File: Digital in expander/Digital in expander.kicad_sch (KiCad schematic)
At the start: 60 parts, among them J1 Screw_Terminal_01x02, J10 Screw_Terminal_01x02, J11 Screw_Terminal_01x02, J12 Screw_Terminal_01x02, J13 Screw_Terminal_01x02, J14 Screw_Terminal_01x02, J15 Screw_Terminal_01x02, J16 Screw_Terminal_01x02, J17 Conn_01x04_Pin, J18 Conn_01x04_Pin, J19 Conn_01x04_Pin, J2 Screw_Terminal_01x02, J20 Conn_01x04_Pin, J21 Conn_01x04_Pin, J22 Conn_01x03_Pin, J3 Screw_Terminal_01x02, J4 Screw_Terminal_01x02, J5 Screw_Terminal_01x02, J6 Screw_Terminal_01x02, J7 Screw_Terminal_01x02, J8 Screw_Terminal_01x02, J9 Screw_Terminal_01x02, U1 PC847, U2 PC847, U3 PC847, U4 PC847, U5 MCP23017_SO

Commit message: Nu borde det fungera bättre
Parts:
- removed J1, J10, J11, J12, J13, J14, J15, J16, J2, J3, J4, J5, J6, J7, J8, J9: Screw_Terminal_01x02, symbol Connector:Screw_Terminal_01x02
- removed R18, R21, R24, R25, R26, R27, R28, R29, R30, R31, R32: 4,7k, symbol Device:R
- added J1, J2: Screw_Terminal_01x16, symbol Connector:Screw_Terminal_01x16
- added J3, J4: Conn_01x15_Pin, symbol Connector:Conn_01x15_Pin
- added R1, R10, R11, R13, R14, R16, R2, R4, R5, R7, R8: 4,7k, symbol Device:R
- renumbered J19 to J10, J20 to J5, J21 to J6, J22 to J7, J17 to J8, J18 to J9, R4 to R12, R5 to R15, R6 to R18, R7 to R21, R8 to R24, R9 to R25, R10 to R26, R11 to R27, R12 to R28, R13 to R29, R1 to R3, R14 to R30, R15 to R31, R16 to R32, R2 to R6, R3 to R9
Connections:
- net at U1.15, U5.1 (GPB0): now also R1.1; no longer R17.1
- net at C1.2, J10.1 (Pin_1), J10.2 (Pin_2)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: now also R1.2, R10.2, R11.2, R13.2, R14.2, R16.2, R2.2, R4.2, R5.2, R7.2, R8.2
- net at U2.15, U5.5 (GPB4): now also R7.1
- net at R15.1: now also J1.5 (Pin_5)
- net at U1.10, U1.12, U1.14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: no longer C1.1, J5.1 (Pin_1), J6.1 (Pin_1), J8.1 (Pin_1), J8.2 (Pin_2), J8.3 (Pin_3), J8.4 (Pin_4), U5.9 (VDD)
- net at R26.1: now also J1.10 (Pin_10)
- net at U4.15, U5.25 (GPA4): now also R19.1
- net at U4.2: now also J2.13 (Pin_13), J3.12 (Pin_12)
- net at R32.1: now also J1.16 (Pin_16)
- net at U4.8: now also J2.16 (Pin_16), J3.15 (Pin_15)
- net at U4.9, U5.28 (GPA7): now also R23.1
- net at R30.1: now also J1.14 (Pin_14)
- net at U4.4: now also J2.14 (Pin_14), J3.13 (Pin_13)
- net at U5.15 (A0): now also J9.2 (Pin_2); no longer J9.1 (Pin_1)
- net at U5.16 (A1): now also J9.3 (Pin_3); no longer J9.2 (Pin_2)
- net at U5.17 (A2): now also J9.4 (Pin_4); no longer J9.3 (Pin_3)
- net at J7.3 (Pin_3), U5.18 (~{RESET}): now also J9.1 (Pin_1); no longer J9.4 (Pin_4)
- net at U1.13, U5.2 (GPB1): now also R2.1
- net at U3.15, U5.21 (GPA0): now also R13.1
- net at U3.13, U5.22 (GPA1): now also R14.1
- net at U3.11, U5.23 (GPA2): now also R16.1
- net at U3.9, U5.24 (GPA3): now also R17.1
- net at U4.13, U5.26 (GPA5): now also R20.1
- net at U4.11, U5.27 (GPA6): now also R22.1
- net at U1.11, U5.3 (GPB2): now also R4.1; no longer R19.1
- net at U1.9, U5.4 (GPB3): now also R5.1; no longer R20.1
- net at U2.13, U5.6 (GPB5): now also R8.1; no longer R22.1
- net at U2.11, U5.7 (GPB6): now also R10.1; no longer R23.1
- net at U2.9, U5.8 (GPB7): now also R11.1
- net at R3.1: now also J1.1 (Pin_1)
- net at R25.1: now also J1.9 (Pin_9)
- net at R28.1: now also J1.12 (Pin_12)
- net at R27.1: now also J1.11 (Pin_11)
- net at U3.6: now also J2.11 (Pin_11), J3.10 (Pin_10)
- net at R24.1: now also J1.8 (Pin_8)
- net at R9.1: now also J1.3 (Pin_3)
- net at U1.6: now also J2.3 (Pin_3), J3.2 (Pin_2)
- net at U3.4: now also J2.10 (Pin_10), J3.9 (Pin_9)
- net at U2.8: now also J2.8 (Pin_8), J3.7 (Pin_7)
- net at U2.2: now also J2.5 (Pin_5), J3.4 (Pin_4)
- net at R29.1: now also J1.13 (Pin_13)
- net at U1.2: now also U1.4, J2.2 (Pin_2), J3.1 (Pin_1)
- net at R21.1: now also J1.7 (Pin_7)
- net at U2.6: now also J2.7 (Pin_7), J3.6 (Pin_6)
- net at R6.1: now also J1.2 (Pin_2)
- net at R12.1: now also J1.4 (Pin_4)
- net at U1.8: now also J2.4 (Pin_4), J3.3 (Pin_3)
- net at U2.4: now also J2.6 (Pin_6), J3.5 (Pin_5)
- net at U4.6: now also J2.15 (Pin_15), J3.14 (Pin_14)
- net at U3.8: now also J2.12 (Pin_12), J3.11 (Pin_11)
- net at U3.2: now also J2.9 (Pin_9), J3.8 (Pin_8)
- net at R18.1: now also J1.6 (Pin_6)
- net at R31.1: now also J1.15 (Pin_15)
- new net: J2.1 (Pin_1), J4.1 (Pin_1), J4.10 (Pin_10), J4.11 (Pin_11), J4.12 (Pin_12), J4.13 (Pin_13), J4.14 (Pin_14), J4.15 (Pin_15), J4.2 (Pin_2), J4.3 (Pin_3), J4.4 (Pin_4), J4.5 (Pin_5), J4.6 (Pin_6), J4.7 (Pin_7), J4.8 (Pin_8), J4.9 (Pin_9)
- new net: C1.1, J5.1 (Pin_1), J6.1 (Pin_1), J8.1 (Pin_1), J8.2 (Pin_2), J8.3 (Pin_3), J8.4 (Pin_4), U5.9 (VDD)
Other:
- note added: "GND 1 (C)"
- note added: "GND 10"
- note added: "GND 11"
- note added: "GND 12"
- note added: "GND 13"
- note added: "GND 14"
- note added: "GND 15"
- note added: "GND 16"
- note added: "GND 2"
- note added: "GND 3"
- note added: "GND 4"
- note added: "GND 5"
- note added: "GND 6"
- note added: "GND 7"
- note added: "GND 8"
- note added: "GND 9"
- moved on the sheet: C1, J10, J5, J6, J7, J8, J9, R12, R15, R18, R21, R24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

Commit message: Förbättrad läsbarhet
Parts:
- R1, R10, R11, R13, R14, R16, R2, R4, R5, R7, R8: value 4,7k -> 1k
- R18, R21, R24, R25, R26, R27, R28, R29, R30, R31, R32: value 1k -> 4,7k
- renumbered J7 to J10, J8 to J5, J9 to J6, J10 to J7, J5 to J8, J6 to J9
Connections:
- net at J4.1 (Pin_1), J4.10 (Pin_10), J4.11 (Pin_11)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: now also J1.1 (Pin_1), U1.2; no longer J2.1 (Pin_1)
- net at J3.9 (Pin_9), U3.4: now also J1.10 (Pin_10); no longer J2.10 (Pin_10)
- net at J3.10 (Pin_10), U3.6: now also J1.11 (Pin_11); no longer J2.11 (Pin_11)
- net at J3.11 (Pin_11), U3.8: now also J1.12 (Pin_12); no longer J2.12 (Pin_12)
- net at J3.12 (Pin_12), U4.2: now also J1.13 (Pin_13); no longer J2.13 (Pin_13)
- net at J3.13 (Pin_13), U4.4: now also J1.14 (Pin_14); no longer J2.14 (Pin_14)
- net at J3.14 (Pin_14), U4.6: now also J1.15 (Pin_15); no longer J2.15 (Pin_15)
- net at J3.15 (Pin_15), U4.8: now also J1.16 (Pin_16); no longer J2.16 (Pin_16)
- net at J3.1 (Pin_1), U1.4: now also J1.2 (Pin_2); no longer J2.2 (Pin_2), U1.2
- net at J3.2 (Pin_2), U1.6: now also J1.3 (Pin_3); no longer J2.3 (Pin_3)
- net at J3.3 (Pin_3), U1.8: now also J1.4 (Pin_4); no longer J2.4 (Pin_4)
- net at J3.4 (Pin_4), U2.2: now also J1.5 (Pin_5); no longer J2.5 (Pin_5)
- net at J3.5 (Pin_5), U2.4: now also J1.6 (Pin_6); no longer J2.6 (Pin_6)
- net at J3.6 (Pin_6), U2.6: now also J1.7 (Pin_7); no longer J2.7 (Pin_7)
- net at J3.7 (Pin_7), U2.8: now also J1.8 (Pin_8); no longer J2.8 (Pin_8)
- net at J3.8 (Pin_8), U3.2: now also J1.9 (Pin_9); no longer J2.9 (Pin_9)
- net at R15.1: now also J2.15 (Pin_15); no longer J1.5 (Pin_5)
- net at R15.2: now also U4.5; no longer U2.1
- net at C1.1, J5.1 (Pin_1), J5.2 (Pin_2)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: now also U1.10, U1.12, U1.14, U1.16, U2.10, U2.12, U2.14, U2.16, U3.10, U3.12, U3.14, U3.16, U4.10, U4.12, U4.14, U4.16
- net at C1.2, J7.1 (Pin_1), J7.2 (Pin_2)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: now also R18.2, R21.2, R24.2, R25.2, R26.2, R27.2, R28.2, R29.2, R30.2, R31.2, R32.2; no longer R1.2, R10.2, R11.2, R13.2, R14.2, R16.2, R2.2, R4.2, R5.2, R7.2, R8.2
- net at R26.1: now also U3.13, U5.22 (GPA1); no longer J1.10 (Pin_10)
- net at U3.3: now also R10.2; no longer R26.2
- net at U3.15, U5.21 (GPA0): now also R25.1; no longer R13.1
- net at U4.1: now also R13.2; no longer R29.2
- net at U4.15, U5.25 (GPA4): now also R29.1; no longer R19.1
- net at U2.11, U5.7 (GPB6): now also R23.1; no longer R10.1
- net at U1.15, U5.1 (GPB0): now also R17.1; no longer R1.1
- net at U5.15 (A0): now also J6.1 (Pin_1); no longer J6.2 (Pin_2)
- net at U5.16 (A1): now also J6.2 (Pin_2); no longer J6.3 (Pin_3)
- net at U5.17 (A2): now also J6.3 (Pin_3); no longer J6.4 (Pin_4)
- net at J10.3 (Pin_3), U5.18 (~{RESET}): now also J6.4 (Pin_4); no longer J6.1 (Pin_1)
- net at U1.13, U5.2 (GPB1): now also R18.1; no longer R2.1
- net at U3.11, U5.23 (GPA2): now also R27.1; no longer R16.1
- net at U3.9, U5.24 (GPA3): now also R28.1; no longer R17.1
- net at U4.13, U5.26 (GPA5): now also R30.1; no longer R20.1
- net at U4.11, U5.27 (GPA6): now also R31.1; no longer R22.1
- net at U4.9, U5.28 (GPA7): no longer R23.1
- net at U1.11, U5.3 (GPB2): now also R19.1; no longer R4.1
- net at U1.9, U5.4 (GPB3): now also R20.1; no longer R5.1
- net at U2.15, U5.5 (GPB4): now also R21.1; no longer R7.1
- net at U2.13, U5.6 (GPB5): now also R22.1; no longer R8.1
- net at U2.9, U5.8 (GPB7): now also R24.1; no longer R11.1
- net at R3.1: now also J2.3 (Pin_3); no longer J1.1 (Pin_1)
- net at U1.1: now also R1.2; no longer R3.2
- net at U3.1: now also R9.2; no longer R25.2
- net at U3.7: now also R12.2; no longer R28.2
- net at U2.7: now also R8.2; no longer R24.2
- net at R6.1: now also J2.6 (Pin_6); no longer J1.2 (Pin_2)
- net at R6.2: now also U2.3; no longer U1.3
- net at R32.1: no longer J1.16 (Pin_16)
- net at R9.1: now also J2.9 (Pin_9); no longer J1.3 (Pin_3)
- net at R12.1: now also J2.12 (Pin_12); no longer J1.4 (Pin_4)
- net at U4.3: now also R14.2; no longer R30.2
- net at U4.7: now also R16.2; no longer R32.2
- net at U2.5: now also R7.2; no longer R21.2
- net at U3.5: now also R11.2; no longer R27.2
- net at U1.7: now also R4.2; no longer R12.2
- net at U1.5: now also R3.2; no longer R9.2
- new net: J2.10 (Pin_10), R10.1
- new net: J2.5 (Pin_5), R5.1
- new net: R5.2, U2.1
- new net: R2.2, U1.3
- new net: J2.8 (Pin_8), R8.1
- new net: J2.1 (Pin_1), R1.1
- new net: J2.13 (Pin_13), R13.1
- new net: J2.16 (Pin_16), R16.1
- new net: J2.2 (Pin_2), R2.1
- new net: J2.7 (Pin_7), R7.1
- new net: J2.14 (Pin_14), R14.1
- new net: J2.11 (Pin_11), R11.1
- new net: J2.4 (Pin_4), R4.1
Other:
- moved on the sheet: J10, J5, J6, J7, J8, J9

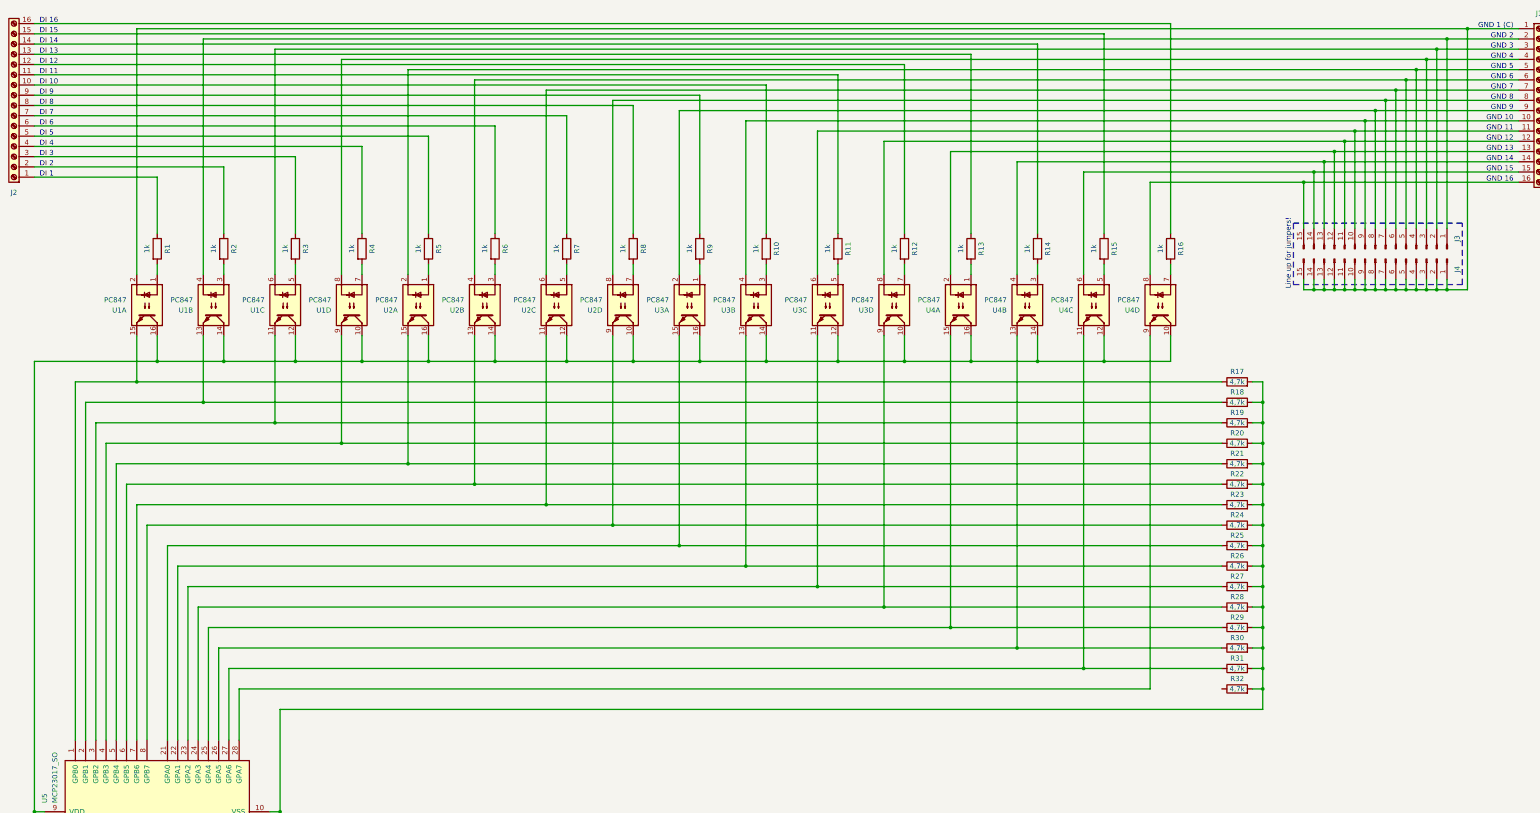
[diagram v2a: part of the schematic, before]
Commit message: Fixat ordning på bitarna
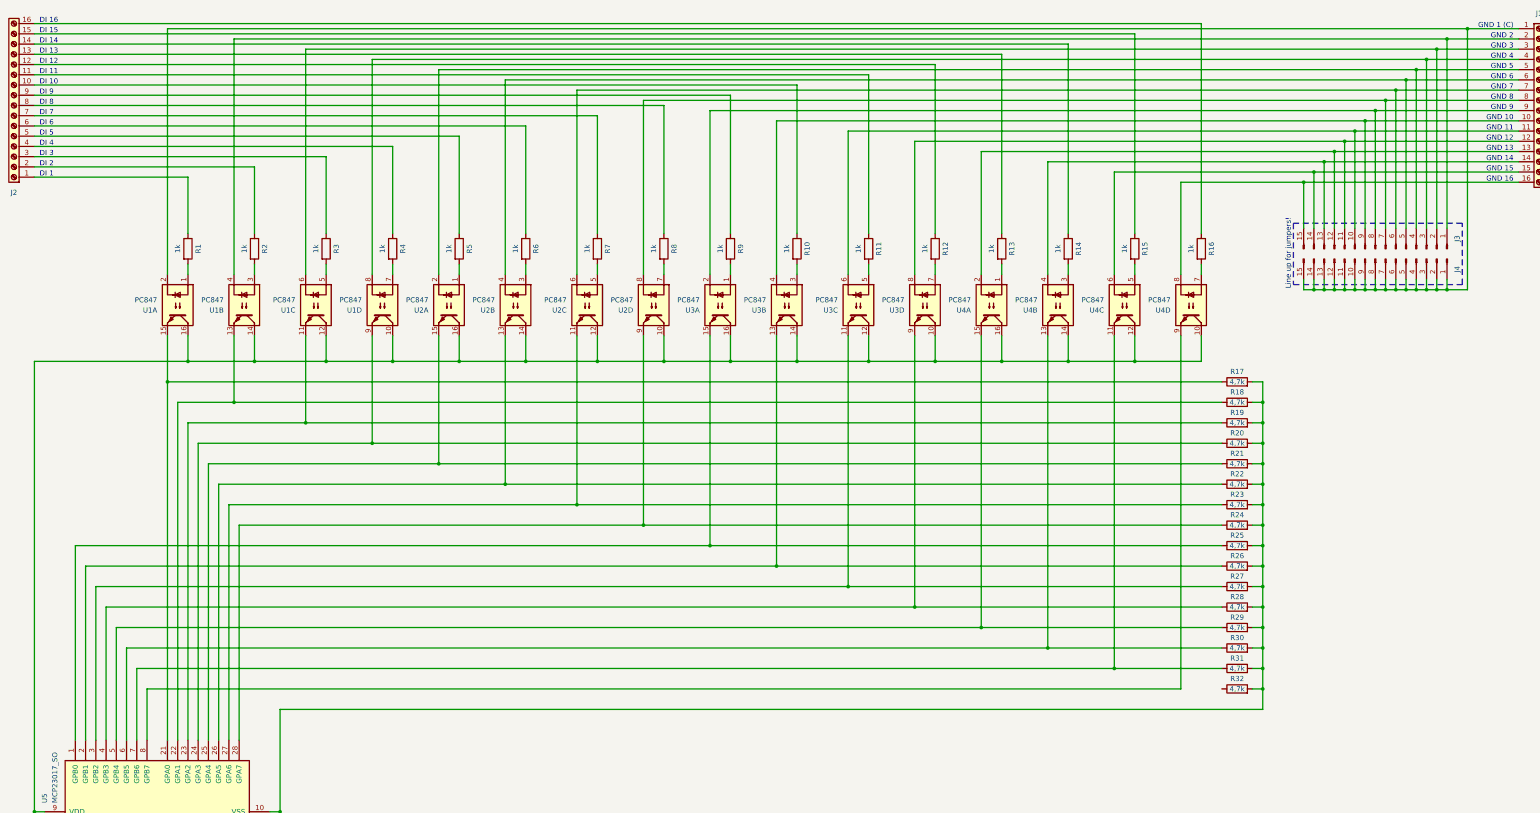
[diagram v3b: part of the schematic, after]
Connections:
- net at R28.1, U3.9: now also U5.4 (GPB3); no longer U5.24 (GPA3)
- net at R22.1, U2.13: now also U5.26 (GPA5); no longer U5.6 (GPB5)
- net at R17.1, U1.15: now also U5.21 (GPA0); no longer U5.1 (GPB0)
- net at R18.1, U1.13: now also U5.22 (GPA1); no longer U5.2 (GPB1)
- net at R25.1, U3.15: now also U5.1 (GPB0); no longer U5.21 (GPA0)
- net at R26.1, U3.13: now also U5.2 (GPB1); no longer U5.22 (GPA1)
- net at R27.1, U3.11: now also U5.3 (GPB2); no longer U5.23 (GPA2)
- net at R29.1, U4.15: now also U5.5 (GPB4); no longer U5.25 (GPA4)
- net at R30.1, U4.13: now also U5.6 (GPB5); no longer U5.26 (GPA5)
- net at R31.1, U4.11: now also U5.7 (GPB6); no longer U5.27 (GPA6)
- net at U5.28 (GPA7): now also R24.1, U2.9; no longer U4.9
- net at R19.1, U1.11: now also U5.23 (GPA2); no longer U5.3 (GPB2)
- net at R20.1, U1.9: now also U5.24 (GPA3); no longer U5.4 (GPB3)
- net at R21.1, U2.15: now also U5.25 (GPA4); no longer U5.5 (GPB4)
- net at R23.1, U2.11: now also U5.27 (GPA6); no longer U5.7 (GPB6)
- new net: U4.9, U5.8 (GPB7)
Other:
- moved on the sheet: R1, R10, R11, R12, R13, R14, R15, R16, R2, R3, R4, R5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

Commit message: Ändrade jumpers för bättre tydlighet
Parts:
- removed C1: 100n, symbol Device:C
- removed J5, J6, J7: Conn_01x04_Pin, symbol Connector:Conn_01x04_Pin
- removed U5: MCP23017_SO, Package_SO:SOIC-28W_7.5x17.9mm_P1.27mm, symbol Interface_Expansion:MCP23017_SO
- added C2: 100n, symbol Device:C
- added J19, J20, J21, J22: Conn_01x03_Pin, symbol Connector:Conn_01x03_Pin
- added U6: MCP23017_SO, Package_SO:SOIC-28W_7.5x17.9mm_P1.27mm, symbol Interface_Expansion:MCP23017_SO
- renumbered J8 to J23, J9 to J24, J10 to J25
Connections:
- net at J23.1 (Pin_1), J24.1 (Pin_1), U1.10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: now also C2.1, J19.1 (Pin_1), J20.1 (Pin_1), J21.1 (Pin_1), J22.1 (Pin_1), U6.9 (VDD)
- net at R28.1, U3.9: now also U6.4 (GPB3)
- net at R22.1, U2.13: now also U6.26 (GPA5)
- net at R25.1, U3.15: now also U6.1 (GPB0)
- net at J23.2 (Pin_2), J24.2 (Pin_2), R17.2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: now also C2.2, J19.3 (Pin_3), J20.3 (Pin_3), J21.3 (Pin_3), J22.3 (Pin_3), U6.10 (VSS)
- net at J23.4 (Pin_4), J24.4 (Pin_4): now also U6.12 (SCK)
- net at J23.3 (Pin_3), J24.3 (Pin_3): now also U6.13 (SDA)
- net at J25.3 (Pin_3): now also J22.2 (Pin_2), U6.18 (~{RESET})
- net at J25.1 (Pin_1): now also U6.19 (INTB)
- net at R26.1, U3.13: now also U6.2 (GPB1)
- net at J25.2 (Pin_2): now also U6.20 (INTA)
- net at R17.1, U1.15: now also U6.21 (GPA0)
- net at R18.1, U1.13: now also U6.22 (GPA1)
- net at R19.1, U1.11: now also U6.23 (GPA2)
- net at R20.1, U1.9: now also U6.24 (GPA3)
- net at R21.1, U2.15: now also U6.25 (GPA4)
- net at R23.1, U2.11: now also U6.27 (GPA6)
- net at R24.1, U2.9: now also U6.28 (GPA7)
- net at R27.1, U3.11: now also U6.3 (GPB2)
- net at R29.1, U4.15: now also U6.5 (GPB4)
- net at R30.1, U4.13: now also U6.6 (GPB5)
- net at R31.1, U4.11: now also U6.7 (GPB6)
- net at U4.9: now also U6.8 (GPB7)
- new net: J19.2 (Pin_2), U6.15 (A0)
- new net: J20.2 (Pin_2), U6.16 (A1)
- new net: J21.2 (Pin_2), U6.17 (A2)

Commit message: Nu med mer rätt
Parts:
- removed J3, J4: Conn_01x15_Pin, symbol Connector:Conn_01x15_Pin
- added J10, J11, J12, J13, J14, J15, J16, J17, J18, J19, J20, J21, J22, J23, J9: Conn_01x02_Pin, symbol Connector:Conn_01x02_Pin
- renumbered C2 to C1, J2 to J1, J23 to J2, J1 to J24, J24 to J3, J25 to J4, J19 to J5, J20 to J6, J21 to J7, J22 to J8, U6 to U1, U1 to U2, U2 to U3, U3 to U4, U4 to U5
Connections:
- net at J24.12 (Pin_12), U4.8: now also J19.2 (Pin_2)
- net at J24.6 (Pin_6), U3.4: now also J13.2 (Pin_2)
- net at J24.8 (Pin_8), U3.8: now also J15.2 (Pin_2)
- net at J24.2 (Pin_2), U2.4: now also J9.2 (Pin_2)
- net at J24.11 (Pin_11), U4.6: now also J18.2 (Pin_2)
- net at J24.13 (Pin_13), U5.2: now also J20.2 (Pin_2)
- net at J24.14 (Pin_14), U5.4: now also J21.2 (Pin_2)
- net at J24.15 (Pin_15), U5.6: now also J22.2 (Pin_2)
- net at J24.16 (Pin_16), U5.8: now also J23.2 (Pin_2)
- net at J24.3 (Pin_3), U2.6: now also J10.2 (Pin_2)
- net at J24.4 (Pin_4), U2.8: now also J11.2 (Pin_2)
- net at J24.5 (Pin_5), U3.2: now also J12.2 (Pin_2)
- net at J24.7 (Pin_7), U3.6: now also J14.2 (Pin_2)
- net at J24.9 (Pin_9), U4.2: now also J16.2 (Pin_2)
- net at J24.10 (Pin_10), U4.4: now also J17.2 (Pin_2)
- net at U1.8 (GPB7), U5.9: now also R32.1
- net at J24.1 (Pin_1), U2.2: now also J10.1 (Pin_1), J11.1 (Pin_1), J12.1 (Pin_1), J13.1 (Pin_1), J14.1 (Pin_1), J15.1 (Pin_1), J16.1 (Pin_1), J17.1 (Pin_1), J18.1 (Pin_1), J19.1 (Pin_1), J20.1 (Pin_1), J21.1 (Pin_1), J22.1 (Pin_1), J23.1 (Pin_1), J9.1 (Pin_1)
